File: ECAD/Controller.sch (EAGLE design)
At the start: 27 parts, among them IC1 PIC18F24K504-I/SP, IC2 TMC2208PLATINE, IC3 ENC28J60PLATINEPCB

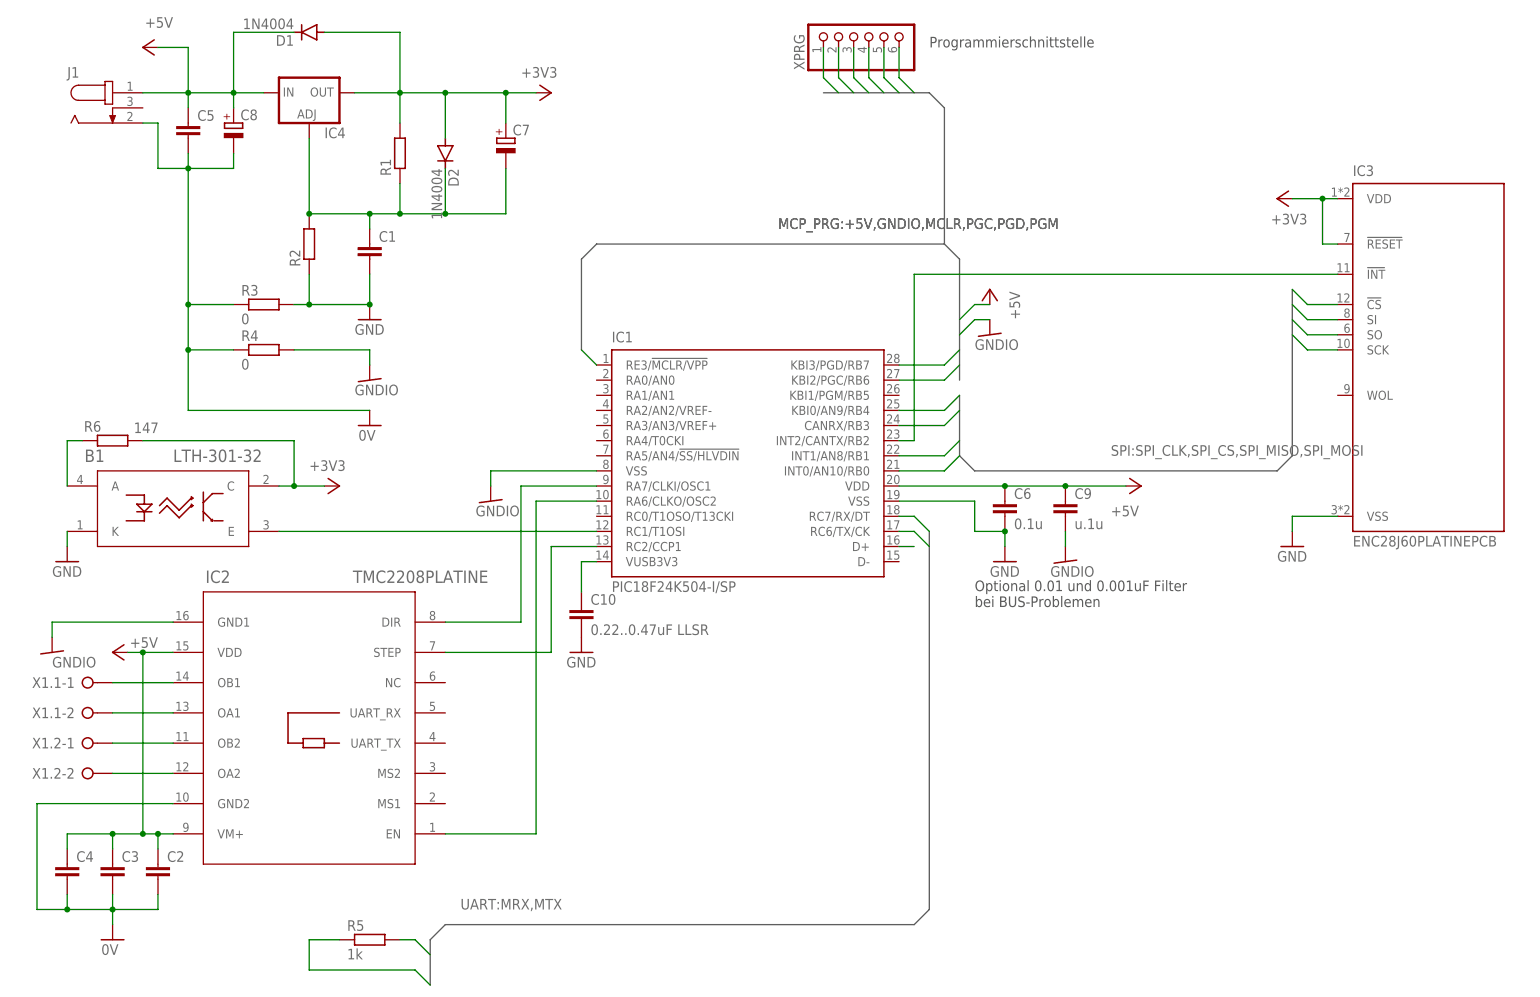
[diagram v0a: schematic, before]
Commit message: Reconfigure MCC, try to reduce memory load
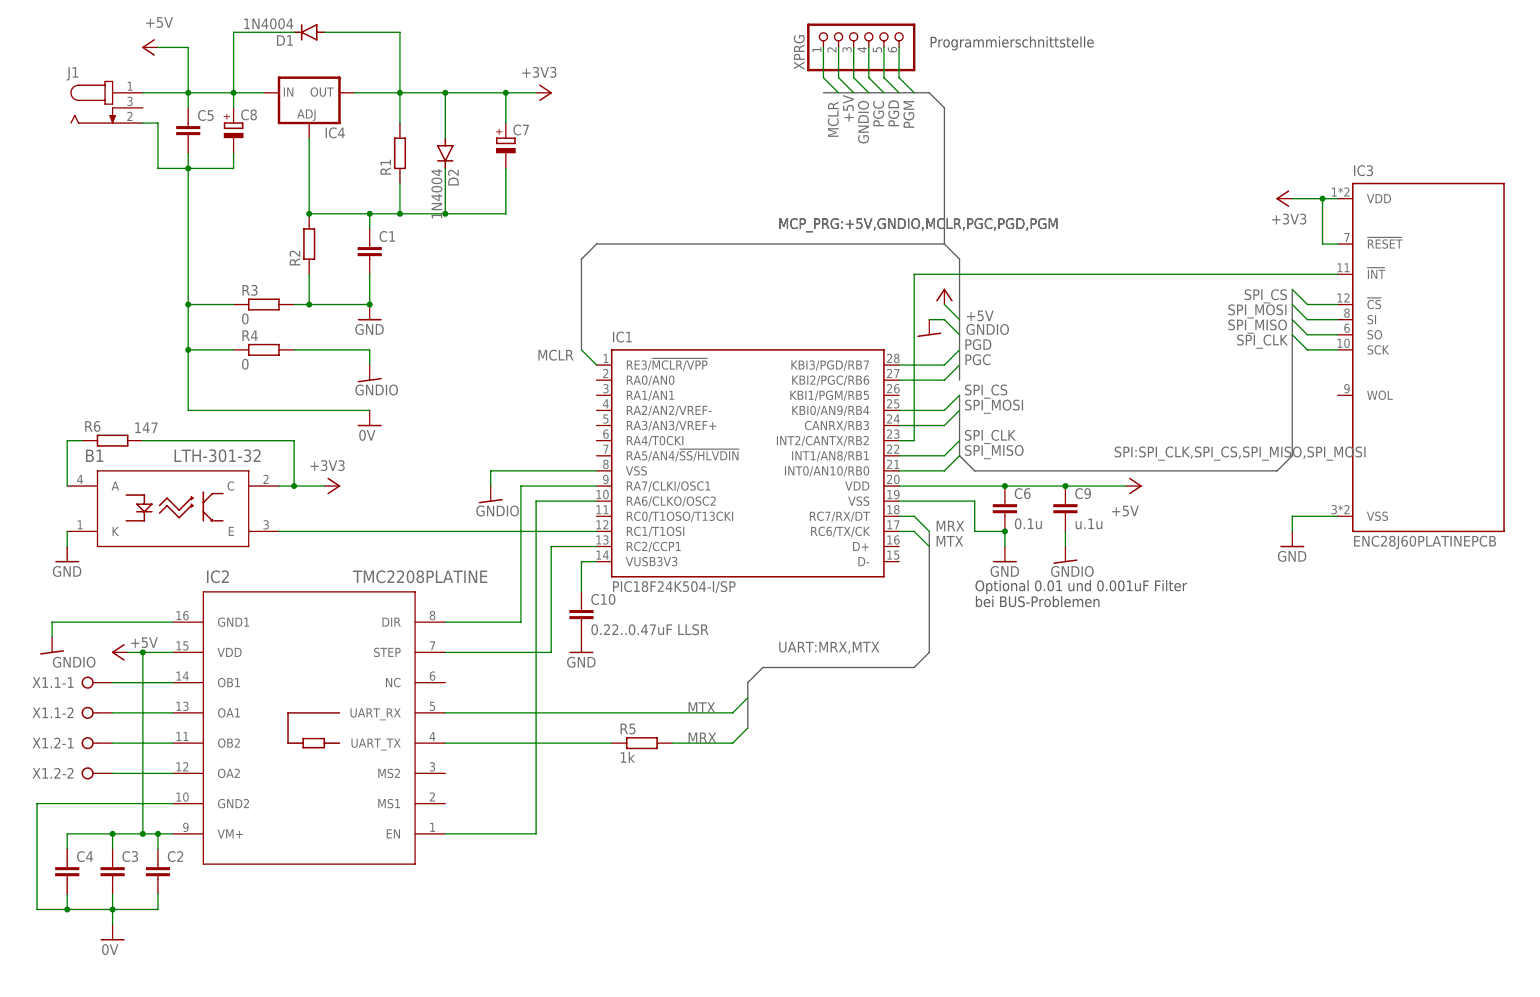
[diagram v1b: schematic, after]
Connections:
- removed net N$11: IC1.D+
- new net N$1: IC2.UART_TX, R5.1
- net MRX: now also R5.2; no longer R5.1
- net MTX: now also IC2.UART_RX; no longer R5.2
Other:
- moved on the sheet: R5
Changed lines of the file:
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@@
 <attribute name="VALUE" x="76.2" y="93.98" size="1.778" layer="96"/>
 </instance>
-<instance part="R5" gate="G$1" x="58.42" y="22.86" smashed="yes">
-<attribute name="NAME" x="54.61" y="24.3586" size="1.778" layer="95"/>
-<attribute name="VALUE" x="54.61" y="19.558" size="1.778" layer="96"/>
+<instance part="R5" gate="G$1" x="104.14" y="55.88" smashed="yes">
+<attribute name="NAME" x="100.33" y="57.3786" size="1.778" layer="95"/>
+<attribute name="VALUE" x="100.33" y="52.578" size="1.778" layer="96"/>
 </instance>
 <instance part="GND8" gate="1" x="165.1" y="86.36" smashed="yes">
@@
 <attribute name="VALUE" x="172.72" y="83.82" size="1.778" layer="96"/>
 </instance>
-<instance part="P+3" gate="1" x="162.56" y="132.08" smashed="yes">
-<attribute name="VALUE" x="167.64" y="127" size="1.778" layer="96" rot="R90"/>
-</instance>
-<instance part="GND10" gate="G$1" x="162.56" y="124.46" smashed="yes">
-<attribute name="VALUE" x="160.02" y="121.92" size="1.778" layer="96"/>
+<instance part="P+3" gate="1" x="154.94" y="132.08" smashed="yes">
+<attribute name="VALUE" x="158.496" y="126.746" size="1.778" layer="96"/>
+</instance>
+<instance part="GND10" gate="G$1" x="152.4" y="124.46" smashed="yes">
+<attribute name="VALUE" x="158.496" y="124.46" size="1.778" layer="96"/>
 </instance>
 <instance part="P+4" gate="1" x="187.96" y="99.06" smashed="yes" rot="R270">
@@
 <wire x1="210.82" y1="101.6" x2="213.36" y2="104.14" width="0.762" layer="92"/>
 <wire x1="213.36" y1="104.14" x2="213.36" y2="132.08" width="0.762" layer="92"/>
-<label x="182.88" y="104.14" size="1.778" layer="95"/>
+<label x="183.388" y="103.886" size="1.778" layer="95"/>
 </segment>
 </bus>
 <bus name="UART:MRX,MTX">
 <segment>
-<wire x1="68.58" y1="15.24" x2="68.58" y2="22.86" width="0.762" layer="92"/>
-<wire x1="68.58" y1="22.86" x2="71.12" y2="25.4" width="0.762" layer="92"/>
-<wire x1="71.12" y1="25.4" x2="149.86" y2="25.4" width="0.762" layer="92"/>
-<wire x1="149.86" y1="25.4" x2="152.4" y2="27.94" width="0.762" layer="92"/>
-<wire x1="152.4" y1="27.94" x2="152.4" y2="91.44" width="0.762" layer="92"/>
-<label x="73.66" y="27.94" size="1.778" layer="95"/>
+<wire x1="121.92" y1="58.42" x2="121.92" y2="66.04" width="0.762" layer="92"/>
+<wire x1="121.92" y1="66.04" x2="124.46" y2="68.58" width="0.762" layer="92"/>
+<wire x1="124.46" y1="68.58" x2="149.86" y2="68.58" width="0.762" layer="92"/>
+<wire x1="149.86" y1="68.58" x2="152.4" y2="71.12" width="0.762" layer="92"/>
+<wire x1="152.4" y1="71.12" x2="152.4" y2="91.44" width="0.762" layer="92"/>
+<label x="127" y="71.12" size="1.778" layer="95"/>
 </segment>
 </bus>
@@
 </segment>
 <segment>
-<wire x1="157.48" y1="124.46" x2="160.02" y2="127" width="0.1524" layer="91"/>
+<wire x1="157.48" y1="124.46" x2="154.94" y2="127" width="0.1524" layer="91"/>
 <pinref part="GND10" gate="G$1" pin="GNDIO"/>
-<wire x1="160.02" y1="127" x2="162.56" y2="127" width="0.1524" layer="91"/>
+<wire x1="154.94" y1="127" x2="152.4" y2="127" width="0.1524" layer="91"/>
 </segment>
 <segment>
@@
 <wire x1="142.24" y1="165.1" x2="139.7" y2="167.64" width="0.1524" layer="91"/>
 <wire x1="139.7" y1="167.64" x2="139.7" y2="172.72" width="0.1524" layer="91"/>
+<label x="142.24" y="156.464" size="1.778" layer="95" rot="R90"/>
 </segment>
 </net>
@@
 </segment>
 <segment>
-<wire x1="157.48" y1="127" x2="160.02" y2="129.54" width="0.1524" layer="91"/>
+<wire x1="157.48" y1="127" x2="154.94" y2="129.54" width="0.1524" layer="91"/>
 <pinref part="P+3" gate="1" pin="+5V"/>
-<wire x1="160.02" y1="129.54" x2="162.56" y2="129.54" width="0.1524" layer="91"/>
 </segment>
 <segment>
@@
 <wire x1="139.7" y1="165.1" x2="137.16" y2="167.64" width="0.1524" layer="91"/>
 <wire x1="137.16" y1="167.64" x2="137.16" y2="172.72" width="0.1524" layer="91"/>
+<label x="139.7" y="160.02" size="1.778" layer="95" rot="R90"/>
 </segment>
 </net>
@@
 <wire x1="147.32" y1="101.6" x2="154.94" y2="101.6" width="0.1524" layer="91"/>
 <wire x1="154.94" y1="101.6" x2="157.48" y2="104.14" width="0.1524" layer="91"/>
+<label x="158.242" y="104.14" size="1.778" layer="95"/>
 </segment>
 <segment>
@@
 <wire x1="213.36" y1="127" x2="215.9" y2="124.46" width="0.1524" layer="91"/>
 <wire x1="215.9" y1="124.46" x2="220.98" y2="124.46" width="0.1524" layer="91"/>
+<label x="212.598" y="127" size="1.778" layer="95" rot="R180"/>
 </segment>
 </net>
@@
 <wire x1="157.48" y1="111.76" x2="154.94" y2="109.22" width="0.1524" layer="91"/>
 <wire x1="154.94" y1="109.22" x2="147.32" y2="109.22" width="0.1524" layer="91"/>
+<label x="158.242" y="111.76" size="1.778" layer="95"/>
 </segment>
 <segment>
@@
 <wire x1="213.36" y1="129.54" x2="215.9" y2="127" width="0.1524" layer="91"/>
 <wire x1="215.9" y1="127" x2="220.98" y2="127" width="0.1524" layer="91"/>
+<label x="212.598" y="129.54" size="1.778" layer="95" rot="R180"/>
 </segment>
 </net>
@@
 <wire x1="157.48" y1="106.68" x2="154.94" y2="104.14" width="0.1524" layer="91"/>
 <wire x1="154.94" y1="104.14" x2="147.32" y2="104.14" width="0.1524" layer="91"/>
+<label x="158.242" y="106.68" size="1.778" layer="95"/>
 </segment>
 <segment>
@@
 <wire x1="213.36" y1="124.46" x2="215.9" y2="121.92" width="0.1524" layer="91"/>
 <wire x1="215.9" y1="121.92" x2="220.98" y2="121.92" width="0.1524" layer="91"/>
+<label x="212.598" y="124.46" size="1.778" layer="95" rot="R180"/>
 </segment>
 </net>
@@
 <wire x1="157.48" y1="114.3" x2="154.94" y2="111.76" width="0.1524" layer="91"/>
 <wire x1="154.94" y1="111.76" x2="147.32" y2="111.76" width="0.1524" layer="91"/>
+<label x="158.242" y="114.3" size="1.778" layer="95"/>
 </segment>
 <segment>
@@
 <wire x1="213.36" y1="132.08" x2="215.9" y2="129.54" width="0.1524" layer="91"/>
 <wire x1="215.9" y1="129.54" x2="220.98" y2="129.54" width="0.1524" layer="91"/>
+<label x="212.598" y="132.08" size="1.778" layer="95" rot="R180"/>
 </segment>
 </net>
@@
 <wire x1="147.32" y1="93.98" x2="149.86" y2="93.98" width="0.1524" layer="91"/>
 <wire x1="152.4" y1="91.44" x2="149.86" y2="93.98" width="0.1524" layer="91"/>
-</segment>
-<segment>
-<pinref part="R5" gate="G$1" pin="1"/>
-<wire x1="48.26" y1="22.86" x2="53.34" y2="22.86" width="0.1524" layer="91"/>
-<wire x1="68.58" y1="15.24" x2="66.04" y2="17.78" width="0.1524" layer="91"/>
-<wire x1="66.04" y1="17.78" x2="48.26" y2="17.78" width="0.1524" layer="91"/>
-<wire x1="48.26" y1="17.78" x2="48.26" y2="22.86" width="0.1524" layer="91"/>
+<label x="153.416" y="91.44" size="1.778" layer="95"/>
+</segment>
+<segment>
+<wire x1="121.92" y1="58.42" x2="119.38" y2="55.88" width="0.1524" layer="91"/>
+<wire x1="109.22" y1="55.88" x2="119.38" y2="55.88" width="0.1524" layer="91"/>
+<label x="111.76" y="55.88" size="1.778" layer="95"/>
+<pinref part="R5" gate="G$1" pin="2"/>
 </segment>
 </net>
@@
 <wire x1="152.4" y1="88.9" x2="149.86" y2="91.44" width="0.1524" layer="91"/>
 <wire x1="149.86" y1="91.44" x2="147.32" y2="91.44" width="0.1524" layer="91"/>
-</segment>
-<segment>
-<pinref part="R5" gate="G$1" pin="2"/>
-<wire x1="68.58" y1="20.32" x2="66.04" y2="22.86" width="0.1524" layer="91"/>
-<wire x1="66.04" y1="22.86" x2="63.5" y2="22.86" width="0.1524" layer="91"/>
+<label x="153.416" y="88.9" size="1.778" layer="95"/>
+</segment>
+<segment>
+<wire x1="121.92" y1="63.5" x2="119.38" y2="60.96" width="0.1524" layer="91"/>
+<label x="111.76" y="60.96" size="1.778" layer="95"/>
+<pinref part="IC2" gate="B" pin="UART_RX"/>
+<wire x1="119.38" y1="60.96" x2="71.12" y2="60.96" width="0.1524" layer="91"/>
 </segment>
 </net>
@@
 <wire x1="157.48" y1="119.38" x2="154.94" y2="116.84" width="0.1524" layer="91"/>
 <wire x1="154.94" y1="116.84" x2="147.32" y2="116.84" width="0.1524" layer="91"/>
+<label x="158.242" y="119.38" size="1.778" layer="95"/>
 </segment>
 <segment>
@@
 <wire x1="144.78" y1="165.1" x2="142.24" y2="167.64" width="0.1524" layer="91"/>
 <wire x1="142.24" y1="167.64" x2="142.24" y2="172.72" width="0.1524" layer="91"/>
+<label x="144.78" y="159.258" size="1.778" layer="95" rot="R90"/>
 </segment>
 </net>
@@
 <wire x1="157.48" y1="121.92" x2="154.94" y2="119.38" width="0.1524" layer="91"/>
 <wire x1="154.94" y1="119.38" x2="147.32" y2="119.38" width="0.1524" layer="91"/>
+<label x="158.242" y="121.92" size="1.778" layer="95"/>
 </segment>
 <segment>
@@
 <wire x1="147.32" y1="165.1" x2="144.78" y2="167.64" width="0.1524" layer="91"/>
 <wire x1="144.78" y1="167.64" x2="144.78" y2="172.72" width="0.1524" layer="91"/>
+<label x="147.32" y="159.258" size="1.778" layer="95" rot="R90"/>
 </segment>
 </net>
@@
 <wire x1="25.4" y1="50.8" x2="15.24" y2="50.8" width="0.1524" layer="91"/>
 <pinref part="X1.2" gate="-2" pin="KL"/>
-</segment>
-</net>
-<net name="N$11" class="0">
-<segment>
-<pinref part="IC1" gate="G$1" pin="D+"/>
-<wire x1="147.32" y1="88.9" x2="149.86" y2="88.9" width="0.1524" layer="91"/>
 </segment>
 </net>
@@
 <pinref part="IC1" gate="G$1" pin="RE3/!MCLR/VPP"/>
 <wire x1="93.98" y1="121.92" x2="96.52" y2="119.38" width="0.1524" layer="91"/>
+<label x="92.71" y="121.92" size="1.778" layer="95" rot="R180"/>
 </segment>
 <segment>
@@
 <wire x1="137.16" y1="165.1" x2="134.62" y2="167.64" width="0.1524" layer="91"/>
 <wire x1="134.62" y1="167.64" x2="134.62" y2="172.72" width="0.1524" layer="91"/>
+<label x="137.16" y="157.48" size="1.778" layer="95" rot="R90"/>
 </segment>
 </net>
@@
 <wire x1="149.86" y1="165.1" x2="147.32" y2="167.64" width="0.1524" layer="91"/>
 <wire x1="147.32" y1="167.64" x2="147.32" y2="172.72" width="0.1524" layer="91"/>
-</segment>
-</net>
+<label x="149.86" y="159.004" size="1.778" layer="95" rot="R90"/>
+</segment>
+</net>
+<net name="N$1" class="0">
+<segment>
+<pinref part="R5" gate="G$1" pin="1"/>
+<pinref part="IC2" gate="B" pin="UART_TX"/>
+<wire x1="99.06" y1="55.88" x2="71.12" y2="55.88" width="0.1524" layer="91"/>
+</segment>
+</net>
